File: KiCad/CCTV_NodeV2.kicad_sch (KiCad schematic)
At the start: 9 parts, among them J1 Solar 6V/10W, J2 Battery (ext, 2× 18650 ||), U1 CN3791, U2 TC4056A_BMS, U3 MT3608, U4 ESP32-S3-DevKitC-1 N16R8, U5 OV7670

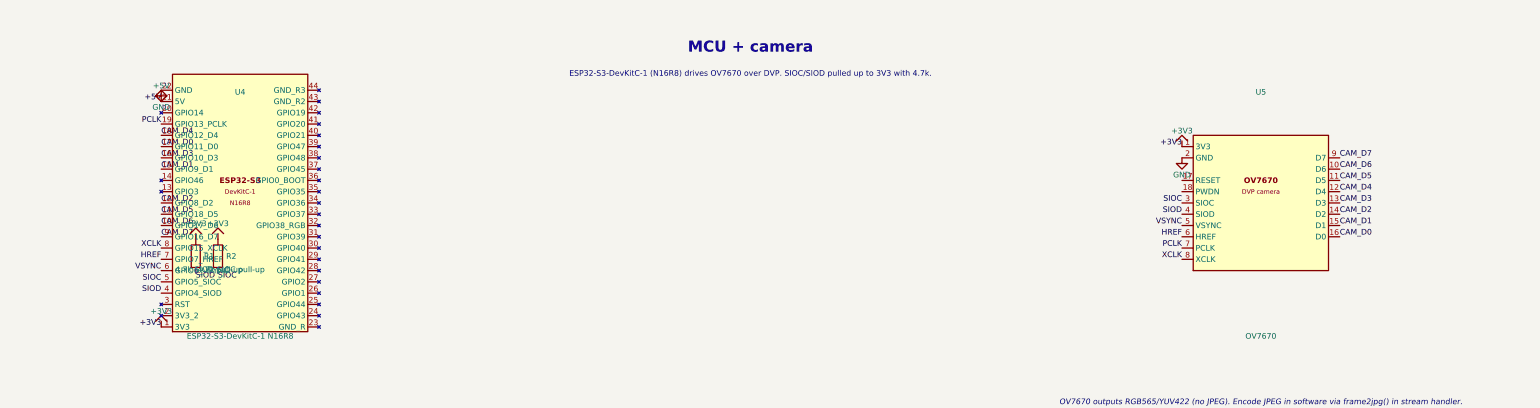
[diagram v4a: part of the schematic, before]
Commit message: Move U4/U5 wiring labels outside component bodies
Previous labels were at x=42.22 (U4 left), x=272.22 (U5 left),
x=307.78 (U5 right) — at the pin stubs but with text potentially
overlapping the component body outline.

New positions (clearly outside all body/courtyard lines):
  U4 left  : x 42.22 → x 15     (29mm clear of body edge at 44.76)
  U5 left  : x 272.22 → x 245   (29mm clear of body edge at 274.76)
  U5 right : x 307.78 → x 330   (24mm clear of body edge at 305.24)

Justify direction:
  Left-side labels  : justify right → text extends LEFT (away from body)
  Right-side labels : justify left  → text extends RIGHT (away from body)

Labels connect by net name within the sheet, so no wires are needed
between label positions and pin stubs.
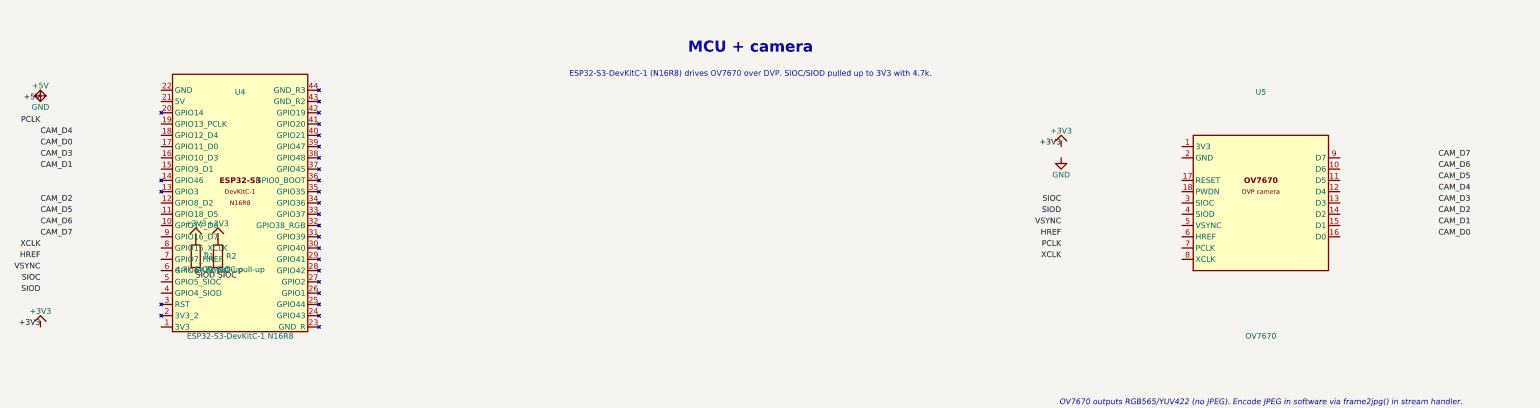
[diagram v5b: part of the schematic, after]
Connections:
- net +3V3: no longer U4.1 (3V3), U5.1 (3V3)
- net +5V: no longer U4.21 (5V)
- net CAM_D0: no longer U4.17 (GPIO11_D0), U5.16 (D0)
- net CAM_D1: no longer U4.15 (GPIO9_D1), U5.15 (D1)
- net CAM_D2: no longer U4.12 (GPIO8_D2), U5.14 (D2)
- net CAM_D3: no longer U4.16 (GPIO10_D3), U5.13 (D3)
- net CAM_D4: no longer U4.18 (GPIO12_D4), U5.12 (D4)
- net CAM_D5: no longer U4.11 (GPIO18_D5), U5.11 (D5)
- net CAM_D6: no longer U4.10 (GPIO17_D6), U5.10 (D6)
- net CAM_D7: no longer U4.9 (GPIO16_D7), U5.9 (D7)
- net GND: no longer U4.22 (GND), U5.2 (GND)
- net HREF: no longer U4.7 (GPIO7_HREF), U5.6 (HREF)
- net PCLK: no longer U4.19 (GPIO13_PCLK), U5.7 (PCLK)
- net SIOC: no longer U4.5 (GPIO5_SIOC), U5.3 (SIOC)
- net SIOD: no longer U4.4 (GPIO4_SIOD), U5.4 (SIOD)
- net VSYNC: no longer U4.6 (GPIO6_VSYNC), U5.5 (VSYNC)
- net XCLK: no longer U4.8 (GPIO15_XCLK), U5.8 (XCLK)
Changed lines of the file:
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@@
 	(symbol
 		(lib_id "CCTV2:+5V")
-		(at 42.22 197.14 0)
+		(at 15 197.14 0)
 		(unit 1)
 		(in_bom yes)
@@
 		(dnp no)
 		(property "Reference" "#PWR02"
-			(at 42.22 193.33 0)
+			(at 15 193.33 0)
 			(hide yes)
 		)
 		(property "Value" "+5V"
-			(at 42.22 193.58 0)
+			(at 15 193.58 0)
 		)
 		(pin "1")
@@
 	(symbol
 		(lib_id "CCTV2:+3V3")
-		(at 42.22 247.94 0)
+		(at 15 247.94 0)
 		(unit 1)
 		(in_bom yes)
@@
 		(dnp no)
 		(property "Reference" "#PWR03"
-			(at 42.22 244.13 0)
+			(at 15 244.13 0)
 			(hide yes)
 		)
 		(property "Value" "+3V3"
-			(at 42.22 244.38 0)
+			(at 15 244.38 0)
 		)
 		(pin "1")
@@
 	(symbol
 		(lib_id "CCTV2:+3V3")
-		(at 272.22 207.30 0)
+		(at 245 207.30 0)
 		(unit 1)
 		(in_bom yes)
@@
 		(dnp no)
 		(property "Reference" "#PWR04"
-			(at 272.22 203.49 0)
+			(at 245 203.49 0)
 			(hide yes)
 		)
 		(property "Value" "+3V3"
-			(at 272.22 203.74 0)
+			(at 245 203.74 0)
 		)
 		(pin "1")
@@
 	(symbol
 		(lib_id "CCTV2:GND")
-		(at 42.22 194.60 0)
+		(at 15 194.60 0)
 		(unit 1)
 		(in_bom yes)
@@
 		(dnp no)
 		(property "Reference" "#PWR14"
-			(at 42.22 200.95 0)
-			(hide yes)
-		)
-		(property "Value" "GND"
-			(at 42.22 198.41 0)
+			(at 15 200.95 0)
+			(hide yes)
+		)
+		(property "Value" "GND"
+			(at 15 198.41 0)
 		)
 		(pin "1")
@@
 	(symbol
 		(lib_id "CCTV2:GND")
-		(at 272.22 209.84 0)
+		(at 245 209.84 0)
 		(unit 1)
 		(in_bom yes)
@@
 		(dnp no)
 		(property "Reference" "#PWR15"
-			(at 272.22 216.19 0)
-			(hide yes)
-		)
-		(property "Value" "GND"
-			(at 272.22 213.65 0)
+			(at 245 216.19 0)
+			(hide yes)
+		)
+		(property "Value" "GND"
+			(at 245 213.65 0)
 		)
 		(pin "1")
@@
 	)
 	(label "+5V"
-		(at 42.22 197.14 0)
+		(at 15 197.14 0)
 		(effects (font (size 1.27 1.27)) (justify right bottom))
 	)
 	(label "+3V3"
-		(at 42.22 247.94 0)
+		(at 15 247.94 0)
 		(effects (font (size 1.27 1.27)) (justify right bottom))
 	)
 	(label "SIOD"
-		(at 42.22 240.32 0)
+		(at 15 240.32 0)
 		(effects (font (size 1.27 1.27)) (justify right bottom))
 	)
 	(label "SIOC"
-		(at 42.22 237.78 0)
+		(at 15 237.78 0)
 		(effects (font (size 1.27 1.27)) (justify right bottom))
 	)
 	(label "VSYNC"
-		(at 42.22 235.24 0)
+		(at 15 235.24 0)
 		(effects (font (size 1.27 1.27)) (justify right bottom))
 	)
 	(label "HREF"
-		(at 42.22 232.70 0)
+		(at 15 232.70 0)
 		(effects (font (size 1.27 1.27)) (justify right bottom))
 	)
 	(label "PCLK"
-		(at 42.22 202.22 0)
+		(at 15 202.22 0)
 		(effects (font (size 1.27 1.27)) (justify right bottom))
 	)
 	(label "XCLK"
-		(at 42.22 230.16 0)
+		(at 15 230.16 0)
 		(effects (font (size 1.27 1.27)) (justify right bottom))
 	)
 	(label "CAM_D0"
-		(at 42.22 207.30 0)
+		(at 15 207.30 0)
 		(effects (font (size 1.27 1.27)) (justify left bottom))
 	)
 	(label "CAM_D1"
-		(at 42.22 212.38 0)
+		(at 15 212.38 0)
 		(effects (font (size 1.27 1.27)) (justify left bottom))
 	)
 	(label "CAM_D2"
-		(at 42.22 220.00 0)
+		(at 15 220.00 0)
 		(effects (font (size 1.27 1.27)) (justify left bottom))
 	)
 	(label "CAM_D3"
-		(at 42.22 209.84 0)
+		(at 15 209.84 0)
 		(effects (font (size 1.27 1.27)) (justify left bottom))
 	)
 	(label "CAM_D4"
-		(at 42.22 204.76 0)
+		(at 15 204.76 0)
 		(effects (font (size 1.27 1.27)) (justify left bottom))
 	)
 	(label "CAM_D5"
-		(at 42.22 222.54 0)
+		(at 15 222.54 0)
 		(effects (font (size 1.27 1.27)) (justify left bottom))
 	)
 	(label "CAM_D6"
-		(at 42.22 225.08 0)
+		(at 15 225.08 0)
 		(effects (font (size 1.27 1.27)) (justify left bottom))
 	)
 	(label "CAM_D7"
-		(at 42.22 227.62 0)
+		(at 15 227.62 0)
 		(effects (font (size 1.27 1.27)) (justify left bottom))
 	)
 	(label "+3V3"
-		(at 272.22 207.30 0)
+		(at 245 207.30 0)
 		(effects (font (size 1.27 1.27)) (justify right bottom))
 	)
 	(label "SIOC"
-		(at 272.22 220.00 0)
+		(at 245 220.00 0)
 		(effects (font (size 1.27 1.27)) (justify right bottom))
 	)
 	(label "SIOD"
-		(at 272.22 222.54 0)
+		(at 245 222.54 0)
 		(effects (font (size 1.27 1.27)) (justify right bottom))
 	)
 	(label "VSYNC"
-		(at 272.22 225.08 0)
+		(at 245 225.08 0)
 		(effects (font (size 1.27 1.27)) (justify right bottom))
 	)
 	(label "HREF"
-		(at 272.22 227.62 0)
+		(at 245 227.62 0)
 		(effects (font (size 1.27 1.27)) (justify right bottom))
 	)
 	(label "PCLK"
-		(at 272.22 230.16 0)
+		(at 245 230.16 0)
 		(effects (font (size 1.27 1.27)) (justify right bottom))
 	)
 	(label "XCLK"
-		(at 272.22 232.70 0)
+		(at 245 232.70 0)
 		(effects (font (size 1.27 1.27)) (justify right bottom))
 	)
 	(label "CAM_D7"
-		(at 307.78 209.84 0)
+		(at 330 209.84 0)
 		(effects (font (size 1.27 1.27)) (justify left bottom))
 	)
 	(label "CAM_D6"
-		(at 307.78 212.38 0)
+		(at 330 212.38 0)
 		(effects (font (size 1.27 1.27)) (justify left bottom))
 	)
 	(label "CAM_D5"
-		(at 307.78 214.92 0)
+		(at 330 214.92 0)
 		(effects (font (size 1.27 1.27)) (justify left bottom))
 	)
 	(label "CAM_D4"
-		(at 307.78 217.46 0)
+		(at 330 217.46 0)
 		(effects (font (size 1.27 1.27)) (justify left bottom))
 	)
 	(label "CAM_D3"
-		(at 307.78 220.00 0)
+		(at 330 220.00 0)
 		(effects (font (size 1.27 1.27)) (justify left bottom))
 	)
 	(label "CAM_D2"
-		(at 307.78 222.54 0)
+		(at 330 222.54 0)
 		(effects (font (size 1.27 1.27)) (justify left bottom))
 	)
 	(label "CAM_D1"
-		(at 307.78 225.08 0)
+		(at 330 225.08 0)
 		(effects (font (size 1.27 1.27)) (justify left bottom))
 	)
 	(label "CAM_D0"
-		(at 307.78 227.62 0)
-		(effects (font (size 1.27 1.27)) (justify left bottom))
-	)
+		(at 330 227.62 0)
+		(effects (font (size 1.27 1.27)) (justify left bottom))
+	)

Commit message: Place U4/U5 labels at pin endpoints (justify right, text extends outward)
Moved labels from the temporary far-out positions (x=15/245/330)
back to the pin endpoints:
  U4 left column  : x = 42.22  (pin endpoint, just outside body at 44.76)
  U5 left column  : x = 272.22 (pin endpoint, just outside body at 274.76)
  U5 right column : x = 307.78 (pin endpoint, just outside body at 305.24)

With 'justify right' on left-side labels, the text renders to the LEFT
of the anchor point (away from the body). With 'justify left' on right-
side labels, text renders to the RIGHT (away from the body). So all
label text is outside the U4/U5 outlines while the connection points
sit exactly at the pin stubs.
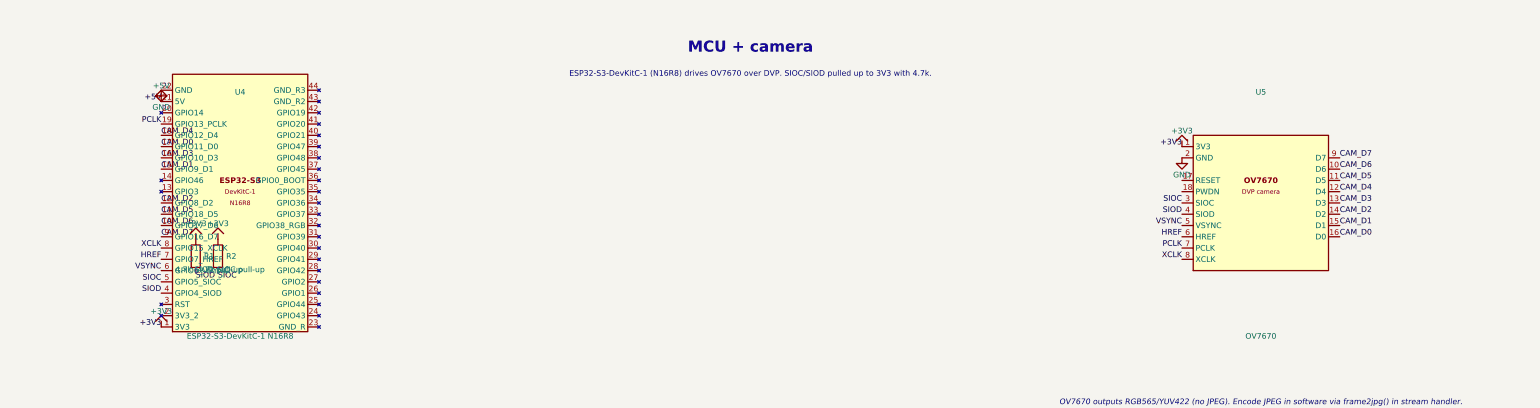
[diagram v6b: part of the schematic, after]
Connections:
- net +3V3: now also U4.1 (3V3), U5.1 (3V3)
- net +5V: now also U4.21 (5V)
- net CAM_D0: now also U4.17 (GPIO11_D0), U5.16 (D0)
- net CAM_D1: now also U4.15 (GPIO9_D1), U5.15 (D1)
- net CAM_D2: now also U4.12 (GPIO8_D2), U5.14 (D2)
- net CAM_D3: now also U4.16 (GPIO10_D3), U5.13 (D3)
- net CAM_D4: now also U4.18 (GPIO12_D4), U5.12 (D4)
- net CAM_D5: now also U4.11 (GPIO18_D5), U5.11 (D5)
- net CAM_D6: now also U4.10 (GPIO17_D6), U5.10 (D6)
- net CAM_D7: now also U4.9 (GPIO16_D7), U5.9 (D7)
- net GND: now also U4.22 (GND), U5.2 (GND)
- net HREF: now also U4.7 (GPIO7_HREF), U5.6 (HREF)
- net PCLK: now also U4.19 (GPIO13_PCLK), U5.7 (PCLK)
- net SIOC: now also U4.5 (GPIO5_SIOC), U5.3 (SIOC)
- net SIOD: now also U4.4 (GPIO4_SIOD), U5.4 (SIOD)
- net VSYNC: now also U4.6 (GPIO6_VSYNC), U5.5 (VSYNC)
- net XCLK: now also U4.8 (GPIO15_XCLK), U5.8 (XCLK)
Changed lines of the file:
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@@
 	(symbol
 		(lib_id "CCTV2:+5V")
-		(at 15 197.14 0)
+		(at 42.22 197.14 0)
 		(unit 1)
 		(in_bom yes)
@@
 		(dnp no)
 		(property "Reference" "#PWR02"
-			(at 15 193.33 0)
+			(at 42.22 193.33 0)
 			(hide yes)
 		)
 		(property "Value" "+5V"
-			(at 15 193.58 0)
+			(at 42.22 193.58 0)
 		)
 		(pin "1")
@@
 	(symbol
 		(lib_id "CCTV2:+3V3")
-		(at 15 247.94 0)
+		(at 42.22 247.94 0)
 		(unit 1)
 		(in_bom yes)
@@
 		(dnp no)
 		(property "Reference" "#PWR03"
-			(at 15 244.13 0)
+			(at 42.22 244.13 0)
 			(hide yes)
 		)
 		(property "Value" "+3V3"
-			(at 15 244.38 0)
+			(at 42.22 244.38 0)
 		)
 		(pin "1")
@@
 	(symbol
 		(lib_id "CCTV2:+3V3")
-		(at 245 207.30 0)
+		(at 272.22 207.30 0)
 		(unit 1)
 		(in_bom yes)
@@
 		(dnp no)
 		(property "Reference" "#PWR04"
-			(at 245 203.49 0)
+			(at 272.22 203.49 0)
 			(hide yes)
 		)
 		(property "Value" "+3V3"
-			(at 245 203.74 0)
+			(at 272.22 203.74 0)
 		)
 		(pin "1")
@@
 	(symbol
 		(lib_id "CCTV2:GND")
-		(at 15 194.60 0)
+		(at 42.22 194.60 0)
 		(unit 1)
 		(in_bom yes)
@@
 		(dnp no)
 		(property "Reference" "#PWR14"
-			(at 15 200.95 0)
-			(hide yes)
-		)
-		(property "Value" "GND"
-			(at 15 198.41 0)
+			(at 42.22 200.95 0)
+			(hide yes)
+		)
+		(property "Value" "GND"
+			(at 42.22 198.41 0)
 		)
 		(pin "1")
@@
 	(symbol
 		(lib_id "CCTV2:GND")
-		(at 245 209.84 0)
+		(at 272.22 209.84 0)
 		(unit 1)
 		(in_bom yes)
@@
 		(dnp no)
 		(property "Reference" "#PWR15"
-			(at 245 216.19 0)
-			(hide yes)
-		)
-		(property "Value" "GND"
-			(at 245 213.65 0)
+			(at 272.22 216.19 0)
+			(hide yes)
+		)
+		(property "Value" "GND"
+			(at 272.22 213.65 0)
 		)
 		(pin "1")
@@
 	)
 	(label "+5V"
-		(at 15 197.14 0)
+		(at 42.22 197.14 0)
 		(effects (font (size 1.27 1.27)) (justify right bottom))
 	)
 	(label "+3V3"
-		(at 15 247.94 0)
+		(at 42.22 247.94 0)
 		(effects (font (size 1.27 1.27)) (justify right bottom))
 	)
 	(label "SIOD"
-		(at 15 240.32 0)
+		(at 42.22 240.32 0)
 		(effects (font (size 1.27 1.27)) (justify right bottom))
 	)
 	(label "SIOC"
-		(at 15 237.78 0)
+		(at 42.22 237.78 0)
 		(effects (font (size 1.27 1.27)) (justify right bottom))
 	)
 	(label "VSYNC"
-		(at 15 235.24 0)
+		(at 42.22 235.24 0)
 		(effects (font (size 1.27 1.27)) (justify right bottom))
 	)
 	(label "HREF"
-		(at 15 232.70 0)
+		(at 42.22 232.70 0)
 		(effects (font (size 1.27 1.27)) (justify right bottom))
 	)
 	(label "PCLK"
-		(at 15 202.22 0)
+		(at 42.22 202.22 0)
 		(effects (font (size 1.27 1.27)) (justify right bottom))
 	)
 	(label "XCLK"
-		(at 15 230.16 0)
+		(at 42.22 230.16 0)
 		(effects (font (size 1.27 1.27)) (justify right bottom))
 	)
 	(label "CAM_D0"
-		(at 15 207.30 0)
+		(at 42.22 207.30 0)
 		(effects (font (size 1.27 1.27)) (justify left bottom))
 	)
 	(label "CAM_D1"
-		(at 15 212.38 0)
+		(at 42.22 212.38 0)
 		(effects (font (size 1.27 1.27)) (justify left bottom))
 	)
 	(label "CAM_D2"
-		(at 15 220.00 0)
+		(at 42.22 220.00 0)
 		(effects (font (size 1.27 1.27)) (justify left bottom))
 	)
 	(label "CAM_D3"
-		(at 15 209.84 0)
+		(at 42.22 209.84 0)
 		(effects (font (size 1.27 1.27)) (justify left bottom))
 	)
 	(label "CAM_D4"
-		(at 15 204.76 0)
+		(at 42.22 204.76 0)
 		(effects (font (size 1.27 1.27)) (justify left bottom))
 	)
 	(label "CAM_D5"
-		(at 15 222.54 0)
+		(at 42.22 222.54 0)
 		(effects (font (size 1.27 1.27)) (justify left bottom))
 	)
 	(label "CAM_D6"
-		(at 15 225.08 0)
+		(at 42.22 225.08 0)
 		(effects (font (size 1.27 1.27)) (justify left bottom))
 	)
 	(label "CAM_D7"
-		(at 15 227.62 0)
+		(at 42.22 227.62 0)
 		(effects (font (size 1.27 1.27)) (justify left bottom))
 	)
 	(label "+3V3"
-		(at 245 207.30 0)
+		(at 272.22 207.30 0)
 		(effects (font (size 1.27 1.27)) (justify right bottom))
 	)
 	(label "SIOC"
-		(at 245 220.00 0)
+		(at 272.22 220.00 0)
 		(effects (font (size 1.27 1.27)) (justify right bottom))
 	)
 	(label "SIOD"
-		(at 245 222.54 0)
+		(at 272.22 222.54 0)
 		(effects (font (size 1.27 1.27)) (justify right bottom))
 	)
 	(label "VSYNC"
-		(at 245 225.08 0)
+		(at 272.22 225.08 0)
 		(effects (font (size 1.27 1.27)) (justify right bottom))
 	)
 	(label "HREF"
-		(at 245 227.62 0)
+		(at 272.22 227.62 0)
 		(effects (font (size 1.27 1.27)) (justify right bottom))
 	)
 	(label "PCLK"
-		(at 245 230.16 0)
+		(at 272.22 230.16 0)
 		(effects (font (size 1.27 1.27)) (justify right bottom))
 	)
 	(label "XCLK"
-		(at 245 232.70 0)
+		(at 272.22 232.70 0)
 		(effects (font (size 1.27 1.27)) (justify right bottom))
 	)
 	(label "CAM_D7"
-		(at 330 209.84 0)
+		(at 307.78 209.84 0)
 		(effects (font (size 1.27 1.27)) (justify left bottom))
 	)
 	(label "CAM_D6"
-		(at 330 212.38 0)
+		(at 307.78 212.38 0)
 		(effects (font (size 1.27 1.27)) (justify left bottom))
 	)
 	(label "CAM_D5"
-		(at 330 214.92 0)
+		(at 307.78 214.92 0)
 		(effects (font (size 1.27 1.27)) (justify left bottom))
 	)
 	(label "CAM_D4"
-		(at 330 217.46 0)
+		(at 307.78 217.46 0)
 		(effects (font (size 1.27 1.27)) (justify left bottom))
 	)
 	(label "CAM_D3"
-		(at 330 220.00 0)
+		(at 307.78 220.00 0)
 		(effects (font (size 1.27 1.27)) (justify left bottom))
 	)
 	(label "CAM_D2"
-		(at 330 222.54 0)
+		(at 307.78 222.54 0)
 		(effects (font (size 1.27 1.27)) (justify left bottom))
 	)
 	(label "CAM_D1"
-		(at 330 225.08 0)
+		(at 307.78 225.08 0)
 		(effects (font (size 1.27 1.27)) (justify left bottom))
 	)
 	(label "CAM_D0"
-		(at 330 227.62 0)
-		(effects (font (size 1.27 1.27)) (justify left bottom))
-	)
+		(at 307.78 227.62 0)
+		(effects (font (size 1.27 1.27)) (justify left bottom))
+	)
